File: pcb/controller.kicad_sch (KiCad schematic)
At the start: 145 parts, among them IC1 TJA1050T_CM,118, IC2 STSPIN32G4, IC3 AS5600-ASOM, IC4 AS5600-ASOM, J1 XT30XT30PW_MALE, J2 XT30XT30PW_MALE, M1 MOUNT, M2 MOUNT, M3 MOUNT, M4 MOUNT, Q1 TPH1R204PLSOP_ADVANCE_8, Q2 TPH1R204PLSOP_ADVANCE_8, Q3 TPH1R204PLSOP_ADVANCE_8, Q4 TPH1R204PLSOP_ADVANCE_8, Q5 TPH1R204PLSOP_ADVANCE_8, Q6 TPH1R204PLSOP_ADVANCE_8, U2 Opamp_Dual, U3 Opamp_Dual, U4 Opamp_Dual

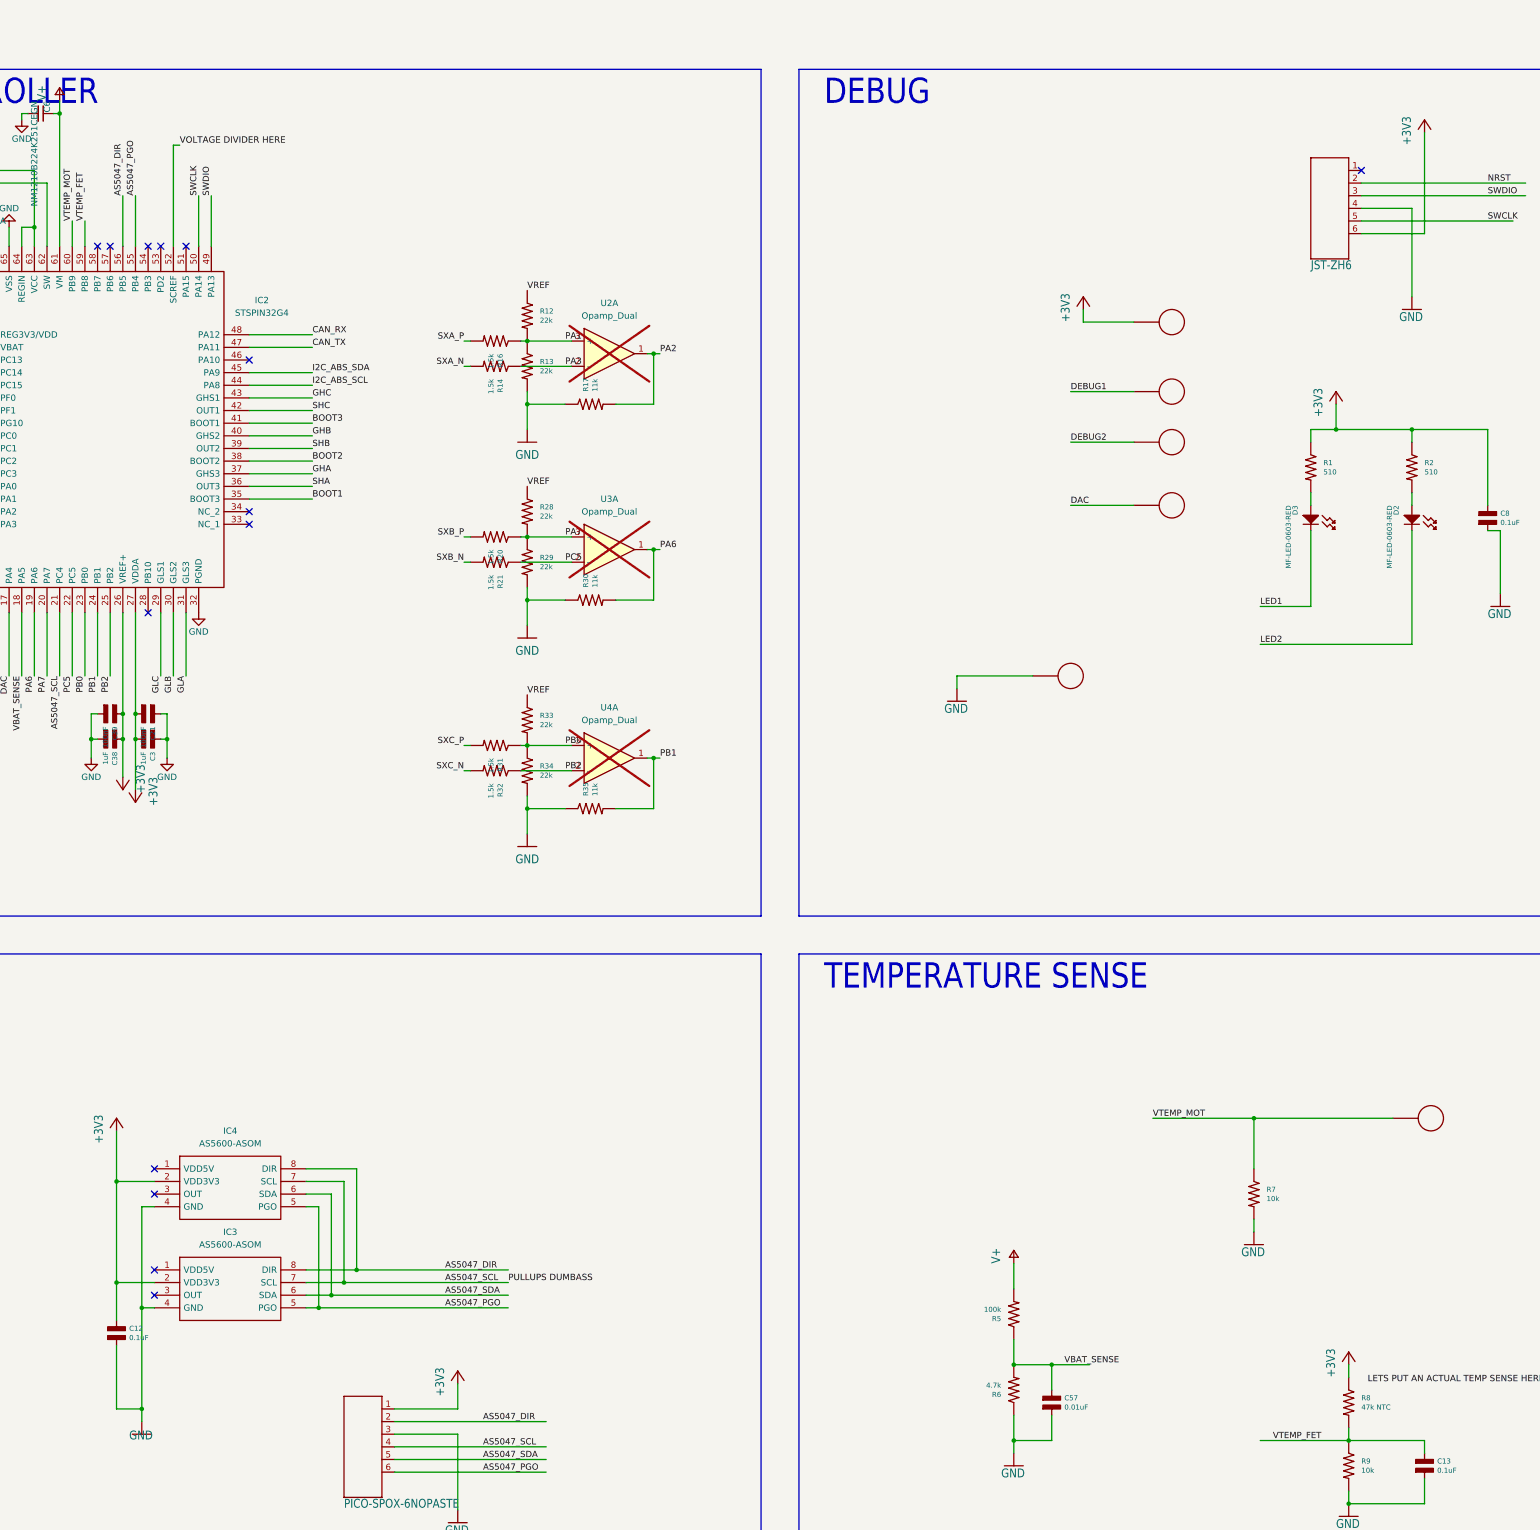
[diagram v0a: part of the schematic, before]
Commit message: Fix op amps, uvlo and thermistor
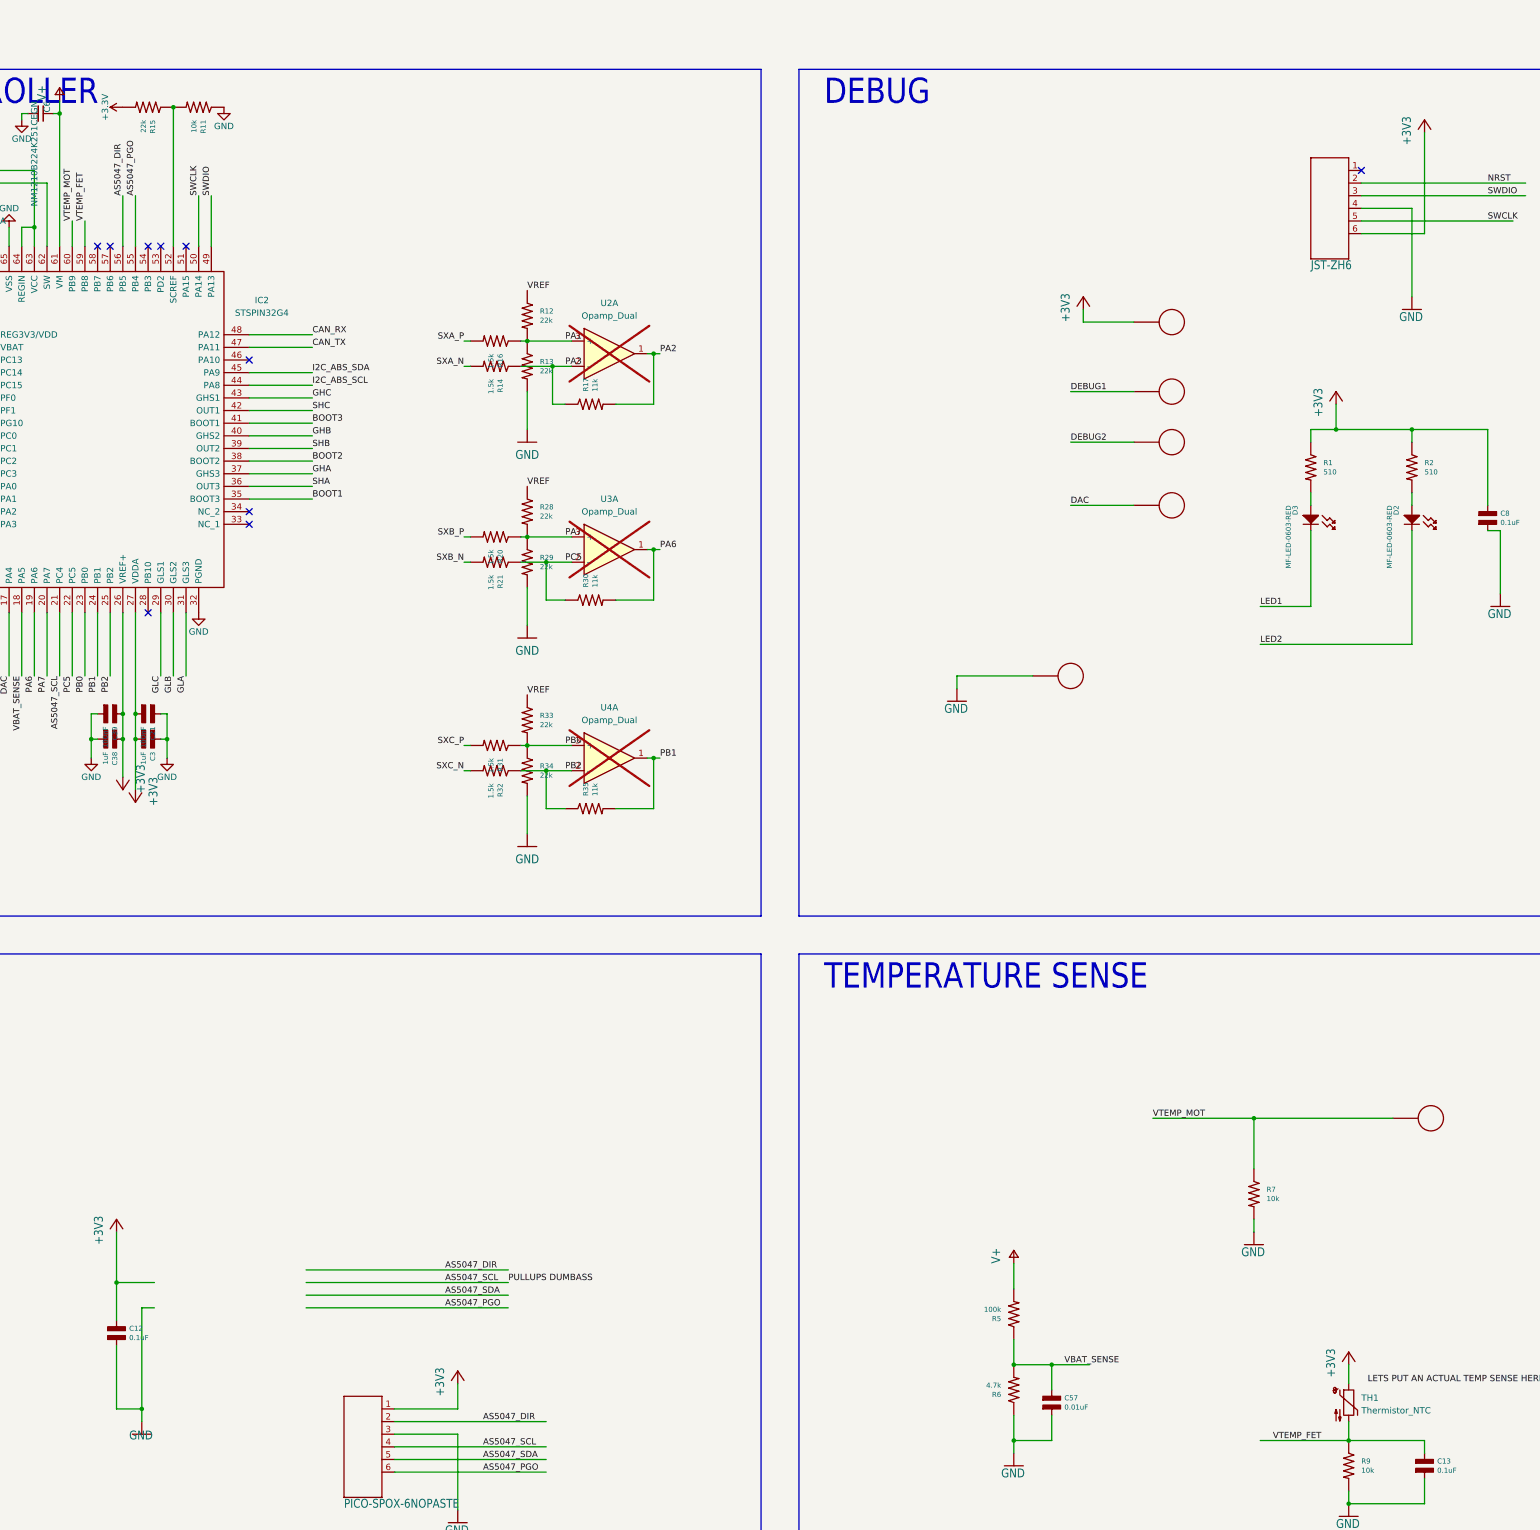
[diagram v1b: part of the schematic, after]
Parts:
- removed IC3, IC4: AS5600-ASOM, SOIC127P600X175-8N, symbol SamacSys:AS5600-ASOM
- removed R8: 47k NTC, controller:R0402, symbol controller-eagle-import:mfpassives_RESISTOR_0402
- added R11: 10k, controller:R0402, symbol controller-eagle-import:mfpassives_RESISTOR_0402
- added R15: 22k, controller:R0402, symbol controller-eagle-import:mfpassives_RESISTOR_0402
- added TH1: Thermistor_NTC, Resistor_SMD:R_0402_1005Metric, symbol Device:Thermistor_NTC
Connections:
- net +3V3: now also R15.P$2, TH1.1
- net GND: now also R11.P$1; no longer R17.P$1, R30.P$1, R35.P$1
- net PA3: now also R17.P$1
- net PB2: now also R35.P$1
- net PC5: now also R30.P$1
- net VTEMP_FET: now also TH1.2
- net VOLTAGE DIVIDER HERE: no longer names the net of IC2.52 (SCREF)
- net VOLTAGE DIVIDER HERE: now also R11.P$2, R15.P$1
- no-connect marks 23 -> 19

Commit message: PCB changes
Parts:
- removed C10, C8: 0.1uF, controller:C0402, symbol controller-eagle-import:mfpassives_CAPACITOR_NP_0402
- removed C11: 0.1uF, controller:C0402_NOBORDER, symbol controller-eagle-import:CAPACITOR_NP_0402_NOBORDER
- removed C55: DNP, controller:C0402, symbol controller-eagle-import:mfpassives_CAPACITOR_NP_0402
- removed C9: 1uF, controller:C0402, symbol controller-eagle-import:mfpassives_CAPACITOR_NP_0402
- removed D33, DAC0, DBG1, DBG2, DG2: PAD24AWG_PAD, controller:24AWG_PAD, symbol controller-eagle-import:PAD24AWG_PAD
- removed IC1: TJA1050T_CM,118, SOIC127P600X175-8N, symbol SamacSys:TJA1050T_CM,118
- removed R10: DNP, controller:R0402, symbol controller-eagle-import:mfpassives_RESISTOR_0402
- removed R14, R21, R32: 1.5k, controller:R0402, symbol controller-eagle-import:mfpassives_RESISTOR_0402
- removed R17, R30, R35: 11k, controller:R0402, symbol controller-eagle-import:mfpassives_RESISTOR_0402
- removed R3, R4: 2k, controller:R0402, symbol controller-eagle-import:mfpassives_RESISTOR_0402
- removed TH1: Thermistor_NTC, Resistor_SMD:R_0402_1005Metric, symbol Device:Thermistor_NTC
- added C1: 100nF, controller:C0402, symbol controller-eagle-import:mfpassives_CAPACITOR_NP_0402
- added C2: 0.1uF, controller:C0402, symbol controller-eagle-import:mfpassives_CAPACITOR_NP_0402
- added JP1: SolderJumper_2_Bridged, Jumper:SolderJumper-2_P1.3mm_Bridged_Pad1.0x1.5mm, symbol Jumper:SolderJumper_2_Bridged
- added JP5: SolderJumper_2_Open, Jumper:SolderJumper-2_P1.3mm_Open_RoundedPad1.0x1.5mm, symbol Jumper:SolderJumper_2_Open
- added JP6, JP7: SolderJumper_3_Bridged12, Jumper:SolderJumper-3_P1.3mm_Bridged12_RoundedPad1.0x1.5mm, symbol Jumper:SolderJumper_3_Bridged12
- added R8: 22k, controller:R0402, symbol controller-eagle-import:mfpassives_RESISTOR_0402
- added TH2: 47k, Resistor_SMD:R_0603_1608Metric, symbol Device:Thermistor_NTC
- added U1: MAX3051, Package_TO_SOT_SMD:TSOT-23-8, symbol Interface_UART:MAX3051
- added U5: AS5048A, Package_SO:TSSOP-14_4.4x5mm_P0.65mm, symbol Sensor_Magnetic:AS5048A
- C12: value 0.1uF -> 10uF
- C14, C19, C20, C6, C7: symbol motor-rescue:C_Small -> Device:C_Small
- R11: value 10k -> 120
- R15: value 22k -> 10k
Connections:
- net SXA_N is gone; now on net PA3: NT8.1
- net SXB_N is gone; now on net PC5: NT1.1
- net SXC_N is gone; now on net PB2: NT6.1
- net +3V3: no longer ABS0.1, C12.P$1, C14.2, C19.2, C20.2, C21.P$2, C3.P$2, C38.P$1, C39.P$1, IC2.1 (REG3V3/VDD), IC2.2 (VBAT), IC2.26 (VREF+), IC2.27 (VDDA), R1.P$1, R15.P$2, R2.P$1, SWD0.6
- net CAN_N: now also R11.P$2, U1.6 (CANL)
- net CAN_P: now also R11.P$1, U1.7 (CANH)
- net CAN_RX: now also JP6.3 (B), JP7.1 (A), U1.4 (RXD); no longer IC2.48 (PA12)
- net CAN_TX: now also JP6.1 (A), JP7.3 (B), U1.1 (TXD); no longer IC2.47 (PA11)
- net GND: now also R1.P$1, R15.P$1, R2.P$1, C1.P$2, C2.P$2, JP1.1 (A), U1.2 (GND), U5.13 (GND), U5.5 (TEST); no longer R11.P$1
- net LED1: now also D3.ANODE; no longer D3.CATHODE
- net LED2: now also D2.ANODE; no longer D2.CATHODE
- net V+: no longer R12.P$1, R28.P$1, R33.P$1
- net VTEMP_FET: now also IC2.58 (PB7), TH2.2; no longer IC2.59 (PB8)
- net VTEMP_MOT: now also IC2.57 (PB6); no longer IC2.60 (PB9)
- net at R2.P$2: now also D2.CATHODE; no longer D2.ANODE
- net at R1.P$2: now also D3.CATHODE; no longer D3.ANODE
- net UART_RXD: now reaches IC2.46 (PA10)
- net UART_RXD: now also ABS0.3
- net AS5048_CS: now reaches IC2.53 (PD2)
- net AS5048_CS: now also ENC0.2, U5.1 (~{CSn})
- net AS5048_SCLK: now reaches IC2.54 (PB3)
- net AS5048_SCLK: now also ENC0.5, U5.2 (CLK)
- net AS5047_DIR renamed AS5048_MOSI
- net AS5048_MOSI: now also ENC0.6, U5.4 (MOSI); no longer ENC0.2
- net AS5047_PGO renamed AS5048_MISO
- net AS5048_MISO: now also ENC0.4, U5.3 (MISO); no longer ENC0.6
- net AS5047_SCL: no longer names the net of IC2.21 (PC4)
- net AS5047_SCL: no longer ENC0.4
- net AS5047_SDA: no longer names the net of IC2.6 (PF0)
- net AS5047_SDA: no longer ENC0.5
- net DAC: no longer names the net of IC2.17 (PA4)
- net I2C_ABS_SCL renamed OUTPUT_PIN
- net OUTPUT_PIN: now also ABS0.1; no longer ABS0.2
- net I2C_ABS_SDA renamed UART_TXD
- net UART_TXD: now also ABS0.2; no longer ABS0.3
- net PA2: no longer names the net of IC2.15 (PA2)
- net PA2: no longer U2.1
- net PA6: no longer names the net of U3.1
- net PA6: no longer IC2.19 (PA6)
- net PB1: no longer names the net of U4.1
- net PB1: no longer IC2.24 (PB1)
- new net: IC2.47 (PA11), JP7.2 (C)
- new net: JP1.2 (B), U1.8 (RS)
- new net: IC2.52 (SCREF), JP5.1 (A), R15.P$2, R8.P$1
- new net: IC2.48 (PA12), JP6.2 (C)
- new net +3.3V: C1.P$1, C12.P$1, C14.2, C19.2, C2.P$1, C20.2, C21.P$2, C3.P$2, C38.P$1, C39.P$1, IC2.1 (REG3V3/VDD), IC2.2 (VBAT), IC2.26 (VREF+), IC2.27 (VDDA), JP5.2 (B), R12.P$1, R28.P$1, R33.P$1, R8.P$2, SWD0.6, TH2.1, U1.3 (VDD), U5.11 (VDD5V), U5.12 (VDD3V)
- no-connect marks 19 -> 31
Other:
- note removed: "Normally a choke goes here but I couldn't find any suitable ones on JLCPCB"
- moved on the sheet: C12, D2, D3, R1, R12, R13, R16, R2, R20, R28, R29, R31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

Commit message: can_monitor - ability to scroll messages - use can send for extended id
main.cpp
- ignore bitrate switching, not needed.
- add can debug messages for all SimpleFOC serial messages
- support extended CAN messages
- reduce current limit
- motor monitoring through CAN

Update schematic and PCB to latest version
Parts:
- removed R20: 1.5k, controller:R0402, symbol controller-eagle-import:mfpassives_RESISTOR_0402
- added R10, R19, R3, R4: 1.5k 1%, Resistor_SMD:R_0402_1005Metric, symbol Device:R_US
- added R14, R17, R18: 11k 1%, Resistor_SMD:R_0402_1005Metric, symbol Device:R_US
- C1, C12, C13, C15, C16, C17, C18, C2, C21, C3, C38, C39, C57: footprint controller:C0402 -> Capacitor_SMD:C_0402_1005Metric; symbol controller-eagle-import:mfpassives_CAPACITOR_NP_0402 -> Device:C_Small
- C22, C23, C24, C25, C26, C27, C28, C29, C30, C31, C32, C33, C34, C36, C37, C61, C63: footprint controller:C1206 -> Capacitor_SMD:C_1206_3216Metric; symbol controller-eagle-import:mfpassives_CAPACITOR_NP_1206 -> Device:C_Small
- C35: footprint controller:C1206_NOBORDER -> Capacitor_SMD:C_1206_3216Metric; symbol controller-eagle-import:CAPACITOR_NP_1206_NOBORDER -> Device:C_Small
- C40, C41, C42, C43, C44, C45, C46, C47, C48, C49, C50, C51, C52, C53, C54: footprint controller:C1206_NOCREAM -> Capacitor_SMD:C_1206_3216Metric; symbol controller-eagle-import:CAPACITOR_NP_1206_NOCREAM -> Device:C_Small
- D2, D3: footprint controller:LED0603 -> LED_SMD:LED_0603_1608Metric; symbol controller-eagle-import:LED_SINGLE-0603-RED -> LED:SFH4346
- M1, M2, M3, M4: footprint MountingHole:MountingHole_2.7mm_M2.5_DIN965_Pad -> MountingHole:MountingHole_3.2mm_M3_DIN965_Pad
- R1, R11, R12, R15, R2, R22, R23, R24, R25, R26, R27, R5, R6, R7, R8, R9: footprint controller:R0402 -> Resistor_SMD:R_0402_1005Metric; symbol controller-eagle-import:mfpassives_RESISTOR_0402 -> Device:R_US
- R13, R28, R29, R33, R34: value 22k -> 22k 1%; footprint controller:R0402 -> Resistor_SMD:R_0402_1005Metric; symbol controller-eagle-import:mfpassives_RESISTOR_0402 -> Device:R_US
- R16, R31: value 1.5k -> 1.5k 1%; footprint controller:R0402 -> Resistor_SMD:R_0402_1005Metric; symbol controller-eagle-import:mfpassives_RESISTOR_0402 -> Device:R_US
- RA0, RB0, RC0: value 0.5mOhm 1% 2W -> 5mOhm 1% 2W; footprint controller:M1206 -> Resistor_SMD:R_1206_3216Metric
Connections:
- net +3.3V: now also C1.1, C12.1, C2.1, C21.2, C3.2, C38.1, C39.1, R12.1, R28.1, R33.1, R8.2; no longer C1.P$1, C12.P$1, C2.P$1, C21.P$2, C3.P$2, C38.P$1, C39.P$1, R12.P$1, R28.P$1, R33.P$1, R8.P$2
- net BOOT1: now also C15.2; no longer C15.P$2
- net BOOT2: now also C17.2; no longer C17.P$2
- net BOOT3: now also C18.2; no longer C18.P$2
- net CAN_N: now also R11.2; no longer R11.P$2
- net CAN_P: now also R11.1; no longer R11.P$1
- net GHA: now also R22.1; no longer R22.P$1
- net GHA_D: now also R22.2; no longer R22.P$2
- net GHB: now also R24.1; no longer R24.P$1
- net GHB_D: now also R24.2; no longer R24.P$2
- net GHC: now also R26.1; no longer R26.P$1
- net GHC_D: now also R26.2; no longer R26.P$2
- net GLA: now also R23.1; no longer R23.P$1
- net GLA_D: now also R23.2; no longer R23.P$2
- net GLB: now also R25.1; no longer R25.P$1
- net GLB_D: now also R25.2; no longer R25.P$2
- net GLC: now also R27.1; no longer R27.P$1
- net GLC_D: now also R27.2; no longer R27.P$2
- net GND: now also C1.2, C12.2, C13.2, C16.2, C2.2, C21.1, C22.2, C23.2, C24.2, C25.2, C26.2, C27.2, C28.2, C29.2, C3.1, C30.2, C31.2, C32.2, C33.2, C34.2, C35.2, C36.2, C37.2, C38.2, C39.2, C40.2, C41.2, C42.2, C43.2, C44.2, C45.2, C46.2, C47.2, C48.2, C49.2, C50.2, C51.2, C52.2, C53.2, C54.2, C57.2, R1.1, R13.2, R15.1, R2.1, R29.2, R34.2, R6.1, R7.2, R9.2; no longer C1.P$2, C12.P$2, C13.P$2, C16.P$2, C2.P$2, C21.P$1, C22.P$2, C23.P$2, C24.P$2, C25.P$2, C26.P$2, C27.P$2, C28.P$2, C29.P$2, C3.P$1, C30.P$2, C31.P$2, C32.P$2, C33.P$2, C34.P$2, C35.P$2, C36.P$2, C37.P$2, C38.P$2, C39.P$2, C40.P$2, C41.P$2, C42.P$2, C43.P$2, C44.P$2, C45.P$2, C46.P$2, C47.P$2, C48.P$2, C49.P$2, C50.P$2, C51.P$2, C52.P$2, C53.P$2, C54.P$2, C57.P$2, R1.P$1, R13.P$2, R15.P$1, R2.P$1, R29.P$2, R34.P$2, R6.P$1, R7.P$2, R9.P$2
- net LED1: now also D3.2 (A); no longer D3.ANODE
- net LED2: now also D2.2 (A); no longer D2.ANODE
- net NRST: now also C16.1; no longer C16.P$1
- net PA1: now also R12.2, R13.1, R16.1; no longer R12.P$2, R13.P$1, R16.P$1
- net PA3: now also R18.2, R4.1; no longer NT8.1
- net PA7: now also R28.2, R29.1, R19.1; no longer R28.P$2, R29.P$1
- net PB0: now also R31.1, R33.2, R34.1; no longer R31.P$1, R33.P$2, R34.P$1
- net PB2: now also R10.1, R14.2; no longer NT6.1
- net PC5: now also R17.2, R3.1; no longer NT1.1
- net SHA: now also C15.1; no longer C15.P$1
- net SHB: now also C17.1; no longer C17.P$1
- net SHC: now also C18.1; no longer C18.P$1
- net SXA_P: now also R16.2; no longer R16.P$2
- net SXB_P: now also R19.2
- net SXC_P: now also R31.2; no longer R31.P$2
- net V+: now also C22.1, C23.1, C24.1, C25.1, C26.1, C27.1, C28.1, C29.1, C30.1, C31.1, C32.1, C33.1, C34.1, C35.1, C36.1, C37.1, C40.1, C41.1, C42.1, C43.1, C44.1, C45.1, C46.1, C47.1, C48.1, C49.1, C50.1, C51.1, C52.1, C53.1, C54.1, C61.1, C63.1, R5.2; no longer C22.P$1, C23.P$1, C24.P$1, C25.P$1, C26.P$1, C27.P$1, C28.P$1, C29.P$1, C30.P$1, C31.P$1, C32.P$1, C33.P$1, C34.P$1, C35.P$1, C36.P$1, C37.P$1, C40.P$1, C41.P$1, C42.P$1, C43.P$1, C44.P$1, C45.P$1, C46.P$1, C47.P$1, C48.P$1, C49.P$1, C50.P$1, C51.P$1, C52.P$1, C53.P$1, C54.P$1, C61.P$1, C63.P$1, R5.P$2
- net VBAT_SENSE: now also C57.1, R5.1, R6.2; no longer C57.P$1, R5.P$1, R6.P$2
- net VTEMP_FET: now also C13.1, R9.1; no longer C13.P$1, R9.P$1
- net VTEMP_MOT: now also R7.1; no longer R7.P$1
- net Z1: now also C61.2; no longer C61.P$2
- net Z3: now also C63.2; no longer C63.P$2
- net PB1: now reaches U4.1
- net PB1: now also IC2.24 (PB1), R14.1
- net PA6: now reaches U3.1
- net PA6: now also IC2.19 (PA6), R17.1
- net at IC2.52 (SCREF), JP5.1 (A): now also R15.2, R8.1; no longer R15.P$2, R8.P$1
- net PA2: now reaches IC2.15 (PA2)
- net PA2: now also U2.1, R18.1
- new net: D2.1 (K), R2.2
- new net: D3.1 (K), R1.2
- new net SXA_N: NT8.1, R4.2
- new net SXB_N: NT1.1, R3.2
- new net SXC_N: NT6.1, R10.2
- no-connect marks 31 -> 25

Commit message: Update schematic to 10mohm shunts
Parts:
- RA0, RB0, RC0: value 5mOhm 1% 2W -> 10mOhm 1% 2W
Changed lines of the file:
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@@
 			)
 		)
-		(property "Value" "5mOhm 1% 2W"
+		(property "Value" "10mOhm 1% 2W"
 			(at 252.222 494.03 0)
 			(effects
@@
 			)
 		)
-		(property "Value" "5mOhm 1% 2W"
+		(property "Value" "10mOhm 1% 2W"
 			(at 300.482 494.03 0)
 			(effects
@@
 			)
 		)
-		(property "Value" "5mOhm 1% 2W"
+		(property "Value" "10mOhm 1% 2W"
 			(at 346.202 494.03 0)
 			(effects
